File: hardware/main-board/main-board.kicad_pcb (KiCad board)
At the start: 4 copper layers, 105 x 38 mm, 88 parts, among them J1 USB_B_Micro, J2 DNI, J3 Display Connector, J4 Conn_01x02, SW1 SW_Push, SW2 SW_Push, SW3 SW_Push, SW4 SW_Push, SW5 SW_Detect, SW6 SW_Boot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

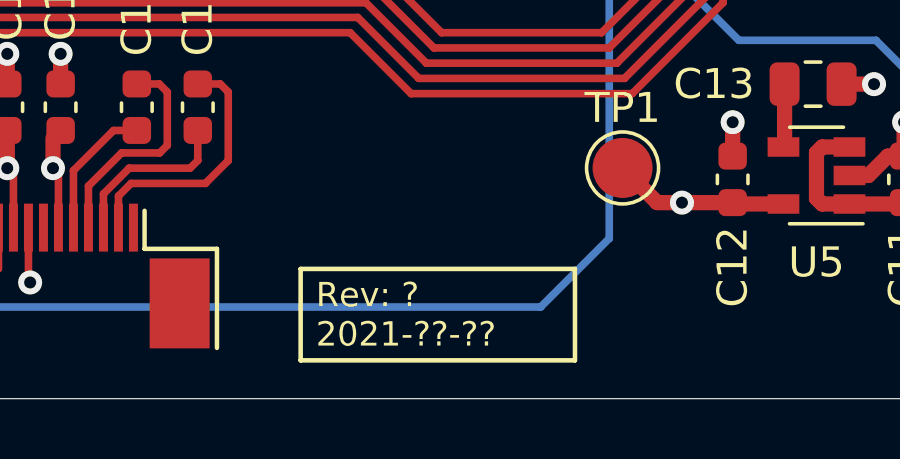
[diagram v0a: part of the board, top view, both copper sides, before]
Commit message: Fixed missing silkscreen date and revision code
Unfortunately this didn't make the prototype fab run, but it will be
there for any future builds.
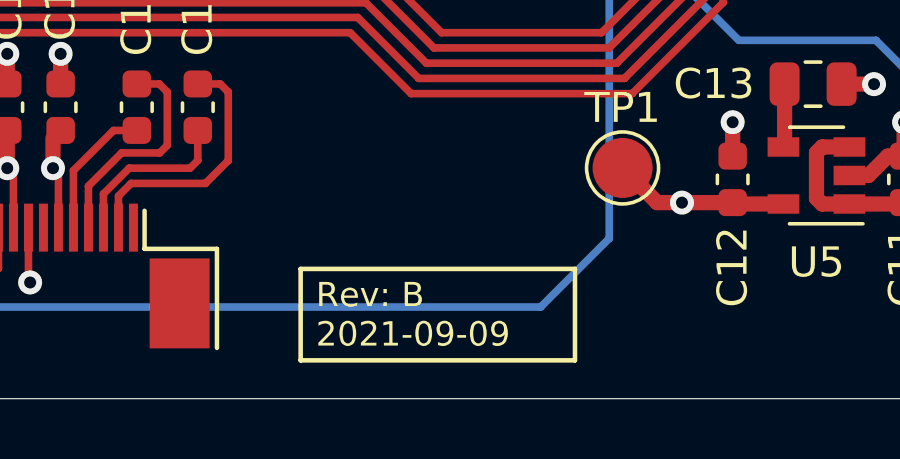
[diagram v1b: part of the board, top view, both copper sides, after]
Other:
- board text added: "Rev: B 2021-09-09"
- board text removed: "Rev: ? 2021-??-??"

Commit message: Fixed ferrite bead component description
Two identical parts should have identical descriptions to make the BOM
data nicer.
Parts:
- FB1: value 600R @ 100MHz -> 600R@100MHz

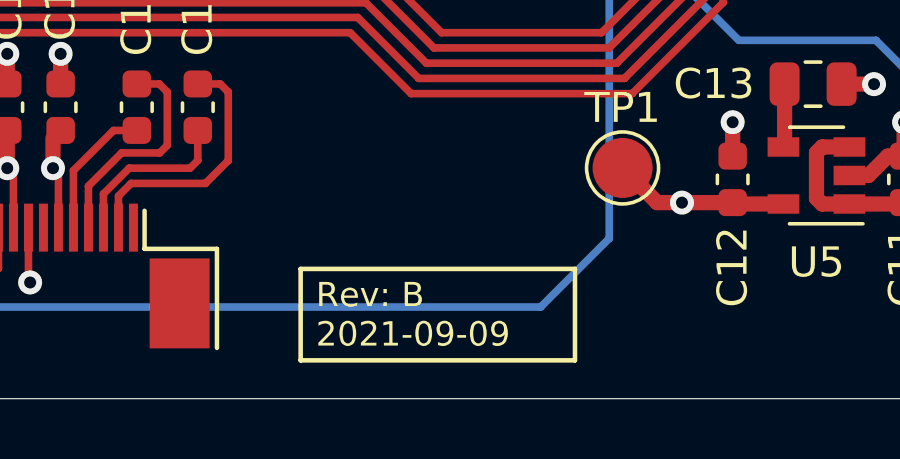
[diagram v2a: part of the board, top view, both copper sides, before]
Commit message: Various title block and metadata updates
- Updated title blocks to show full company name.
- Added Email address
- Added annotation IDs to graphic symbols on the main board, because some
  BOM tools don't really like those being left off.
- Updated revision and date fields for the main board to placeholders in
  preparation for Rev C changes
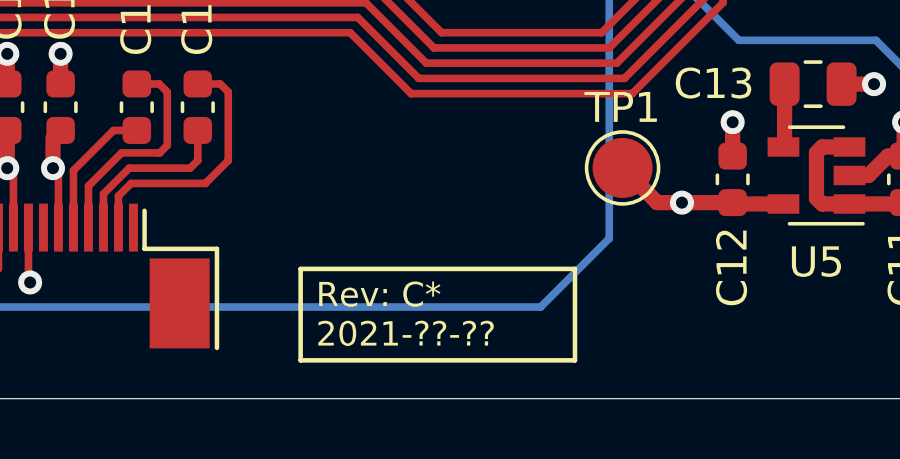
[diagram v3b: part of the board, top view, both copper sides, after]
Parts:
- LOGO: value G*** -> G3
- renumbered G*** to G1, G*** to G2, G*** to G4
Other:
- board text added: "Rev: C* 2021-??-??"
- board text removed: "Rev: B 2021-09-09"
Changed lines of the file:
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@@
-(kicad_pcb (version 20171130) (host pcbnew 5.1.10-88a1d61d58~90~ubuntu21.04.1)
+(kicad_pcb (version 20171130) (host pcbnew 5.1.12-84ad8e8a86~92~ubuntu21.04.1)
   (general
     (thickness 1.6)
@@
   (title_block
     (title "Printalyzer Densitometer - Main Board")
-    (date 2021-09-09)
-    (rev B)
-    (company Dektronics)
-    (comment 1 "Derek Konigsberg")
+    (date 2021-??-??)
+    (rev C*)
+    (company "Dektronics, Inc.")
+    (comment 1 "Derek Konigsberg <dkonigsberg@dektronics.com>")
   )
   (layers
@@
   (module lib_fp:OSHW-logo_5mm (layer B.Cu)
     (at 136.906 48.514)
-    (fp_text reference G*** (at 0 -2.65176) (layer B.SilkS) hide
+    (fp_text reference G4 (at 0 -2.65176) (layer B.SilkS) hide
       (effects (font (size 0.22606 0.22606) (thickness 0.04318)) (justify mirror))
     )
@@
       (effects (font (size 1.524 1.524) (thickness 0.3048)) (justify mirror))
     )
-    (fp_text value G*** (at 0 -2.3) (layer B.SilkS) hide
+    (fp_text value G3 (at 0 -2.3) (layer B.SilkS) hide
       (effects (font (size 1.524 1.524) (thickness 0.3048)) (justify mirror))
     )
@@
   (module lib_fp:densitometer-logo-16_9mm (layer B.Cu)
     (at 124.25 70.976)
-    (fp_text reference G*** (at 0 0) (layer B.SilkS) hide
+    (fp_text reference G2 (at 0 0) (layer B.SilkS) hide
       (effects (font (size 1.524 1.524) (thickness 0.3)) (justify mirror))
     )
@@
   (module lib_fp:Printalyzer-logo-16_9mm (layer B.Cu)
     (at 122.809 74.676)
-    (fp_text reference G*** (at 0 0) (layer B.SilkS) hide
+    (fp_text reference G1 (at 0 0) (layer B.SilkS) hide
       (effects (font (size 1.524 1.524) (thickness 0.3)) (justify mirror))
     )
@@
     (arrow2b (pts (xy 146 33.500001) (xy 144.873496 34.086422)))
   )
-  (gr_text "Rev: B\n2021-09-09" (at 114.284 67.077 180) (layer B.SilkS)
+  (gr_text "Rev: C*\n2021-??-??" (at 114.284 67.077 180) (layer B.SilkS)
     (effects (font (size 0.8128 0.8128) (thickness 0.1524)) (justify left mirror))
   )
@@
   (gr_line (start 107.823 77.724) (end 116.967 77.724) (layer F.SilkS) (width 0.1524))
   (gr_line (start 107.823 74.676) (end 107.823 77.724) (layer F.SilkS) (width 0.1524))
-  (gr_text "Rev: B\n2021-09-09" (at 108.331 76.2) (layer F.SilkS)
+  (gr_text "Rev: C*\n2021-??-??" (at 108.331 76.2) (layer F.SilkS)
     (effects (font (size 0.8128 0.8128) (thickness 0.1524)) (justify left))
   )

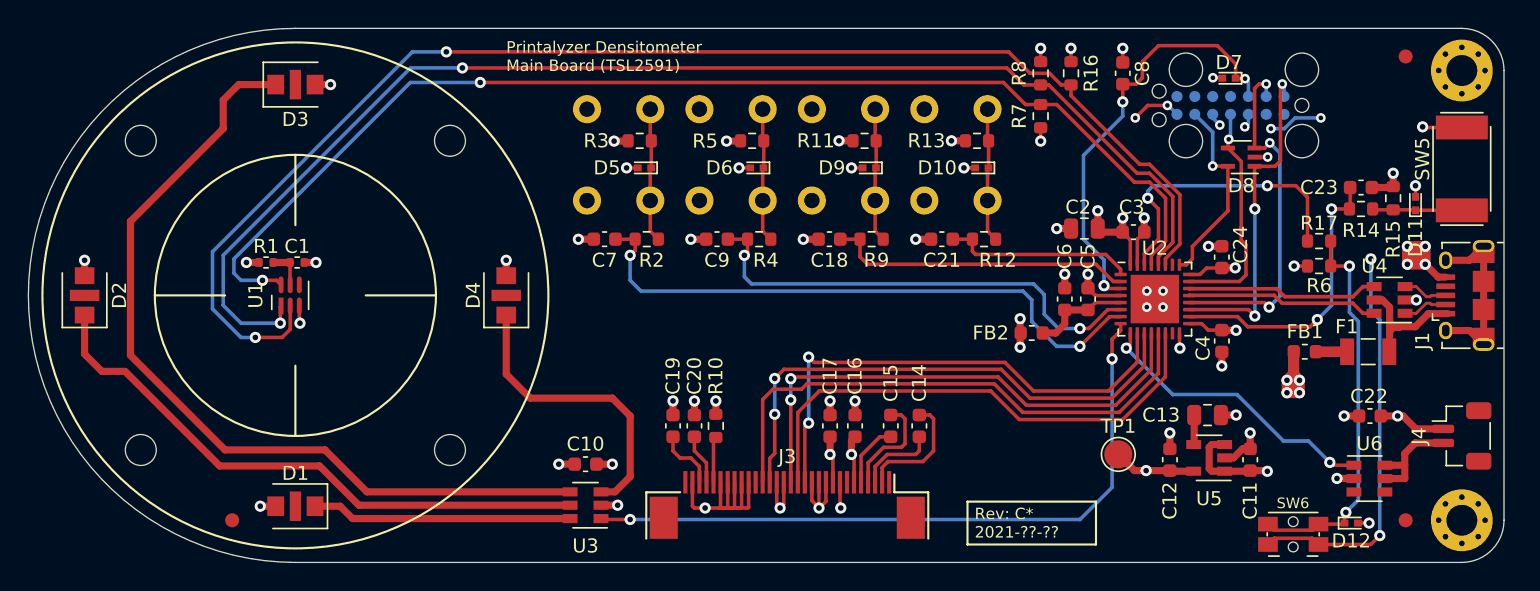
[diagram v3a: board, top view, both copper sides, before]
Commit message: Update LED footprints for thermal properties
Fixes naming convention of thermally-enhanced LED footprints to be
closer to the KiCad convention, and separates into two versions. One
with thermal vias and one without.

Updated transmission board metadata to referene the correct new
footprint name.

Updated main board to use the new version of the new footprint without
thermal vias.

Fixes #22
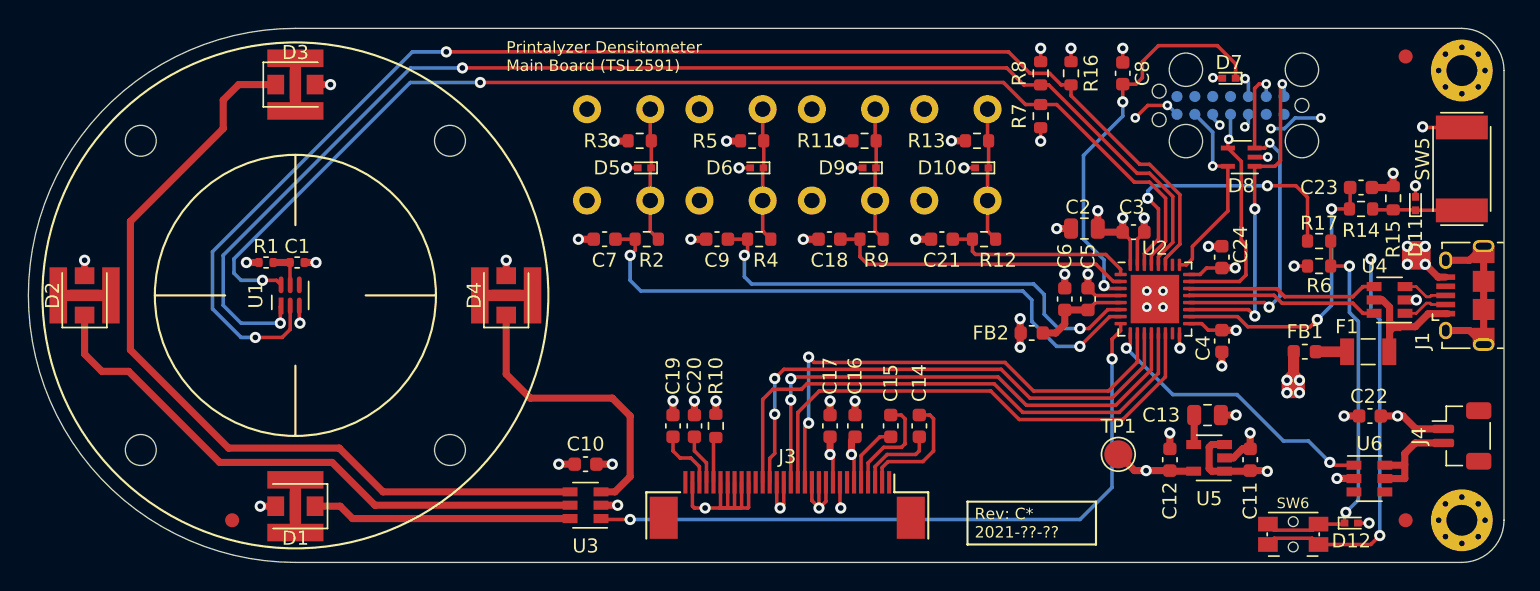
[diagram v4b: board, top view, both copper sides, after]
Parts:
- D1, D2, D3, D4: footprint lib_fp:LED_WL-SWTP-3022 -> lib_fp:LED_WL-SWTP-3022-1MP

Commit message: First pass at updating layout for Rev C component changes
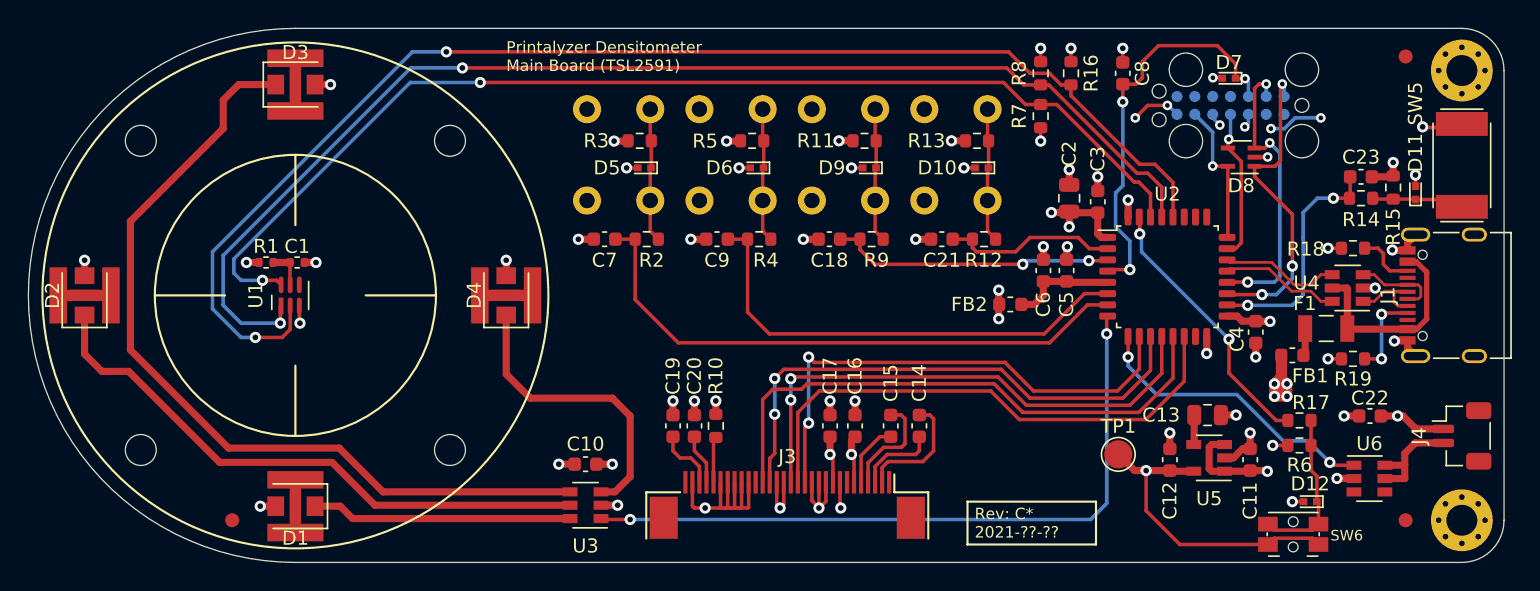
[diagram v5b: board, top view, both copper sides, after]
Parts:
- removed C24: 0.1uF, Capacitor_SMD:C_0603_1608Metric
- added R18: 5.1k, Resistor_SMD:R_0603_1608Metric, F.Cu at (135.3, 56.6)
- added R19: 5.1k, Resistor_SMD:R_0603_1608Metric, F.Cu at (135.3, 64.5)
- J1: value USB_B_Micro -> USB_C_Receptacle_USB2.0; footprint Connector_USB:USB_Micro-B_Amphenol_10118194_Horizontal -> lib_fp:USB_C_Receptacle_GCT_USB4105
- U2: value STM32L072KBU6 -> STM32L072KZT6; footprint Package_DFN_QFN:QFN-32-1EP_5x5mm_P0.5mm_EP3.45x3.45mm -> lib_fp:ST_LQFP32
- moved R6 12.8 mm to (131.4, 70.7)
- moved R17 12.8 mm to (131.4, 68.9)
- moved F1 3.41 mm to (133.3, 62.4)
- moved C3 3.33 mm to (117.1, 53.3), turned to 90 degrees
- moved D12 3.29 mm to (132.2, 74.7), turned to 180 degrees
- moved U4 3.10 mm to (134.9, 59.5)
- moved FB2 2.54 mm to (110.9, 60.6)
- moved C5 2.54 mm to (114.9, 58.2)
- moved C6 2.54 mm to (113.2, 58.2)
- moved C4 2.50 mm to (128.3, 62.6)
- moved C2 2.41 mm to (115.1, 53.1), turned to 90 degrees
- moved U2 1.82 mm to (122.0, 58.7)
- moved J1 1.59 mm to (141.7, 60.0)
- moved FB1 0.92 mm to (130.9, 64.3)
- moved C23 0.76 mm to (135.8, 51.6)
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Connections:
- F1 pad 2: Net-(F1-Pad2) -> VBUS
- U2 pad 1: /BTN4 -> +3V3
- U2 pad 2: /BTN3 -> /BTN4
- U2 pad 24: +3V3 -> /SWCLK
- U2 pad 25: /SWCLK -> Net-(U2-Pad25)
- U2 pad 27: /TSL_INT -> Net-(U2-Pad27)
- U2 pad 28: /I2C1_SCL -> /TSL_INT
- U2 pad 29: /I2C1_SDA -> /I2C1_SCL
- U2 pad 3: /RESET -> /BTN3
- U2 pad 30: /BOOT0 -> /I2C1_SDA
- U2 pad 31: GND -> /BOOT0
- U2 pad 32: +3V3 -> GND
- U2 pad 4: GND -> /RESET
- U4 pad 5: Net-(F1-Pad2) -> VBUS
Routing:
- net Net-(D12-Pad1): track 27.9 -> 11.6 mm, vias 2 -> 0
- net +3V3: track 64.7 -> 48.9 mm, vias 17 -> 14
- net VBUS: track 0.00 -> 14.9 mm
- net Net-(J1-Pad6): track 13.2 -> 0.00 mm
- net Net-(F1-Pad2): track 10.8 -> 0.00 mm
- net GND: track 82.5 -> 73.9 mm, vias 58 -> 54
- net Net-(J1-PadA5): track 0.00 -> 6.45 mm, vias 0 -> 2
- net /SWDIO: track 16.4 -> 10.8 mm
- net /USB_D+: track 13.7 -> 8.51 mm
- net /USB_D-: track 13.7 -> 8.51 mm
- net /I2C1_SDA: track 84.8 -> 80.1 mm
- net /USART1_RX: track 25.5 -> 21.1 mm
- net /I2C1_SCL: track 91.7 -> 87.5 mm
- net Net-(J1-PadB5): track 0.00 -> 4.17 mm
- net /BTN5: track 20.7 -> 16.8 mm
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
